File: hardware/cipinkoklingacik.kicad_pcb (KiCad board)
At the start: 2 copper layers, 100 x 85 mm, 96 parts, among them J1 GLITCH/GND, J2 TARGET/GND, J3 RESET/GND, J4 TRIGGER/GND, J5 UART, Q1 AO3400A, Q2 Si2377EDS, Q3 Si2377EDS, Q4 2N7002, Q5 2N7002, Q6 2N7002, U1 Raspberry Pi Pico 2, U2 UCC27517DBVR, U3 NX3L1T3157GMZ, U4 AP2112K-3.3, U5 AP2112K-1.8, U6 TLV70436DBVR, U7 SN74LVC1G17, U8 SN74AXC4T774PWR

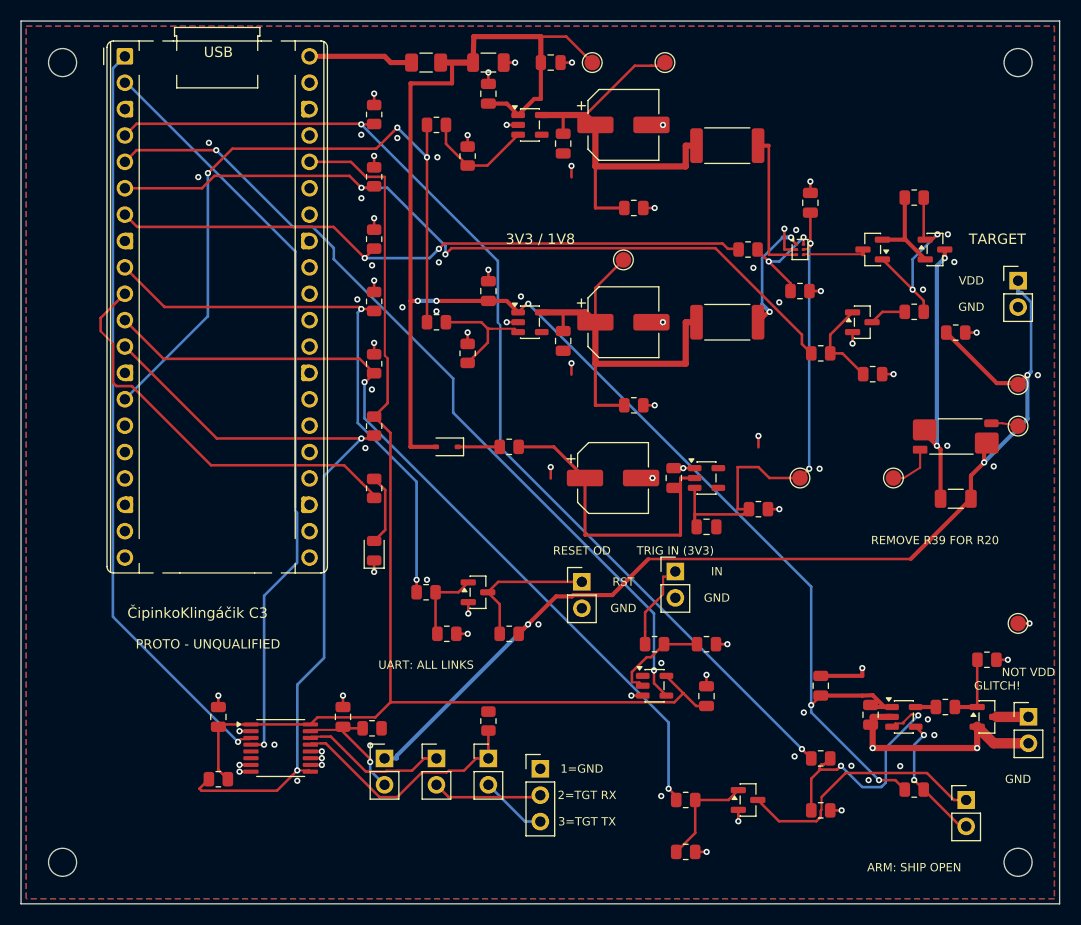
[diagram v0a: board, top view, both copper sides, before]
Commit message: Prepare C4 alpha.2 with stocked sourcing and DFM audit fixes
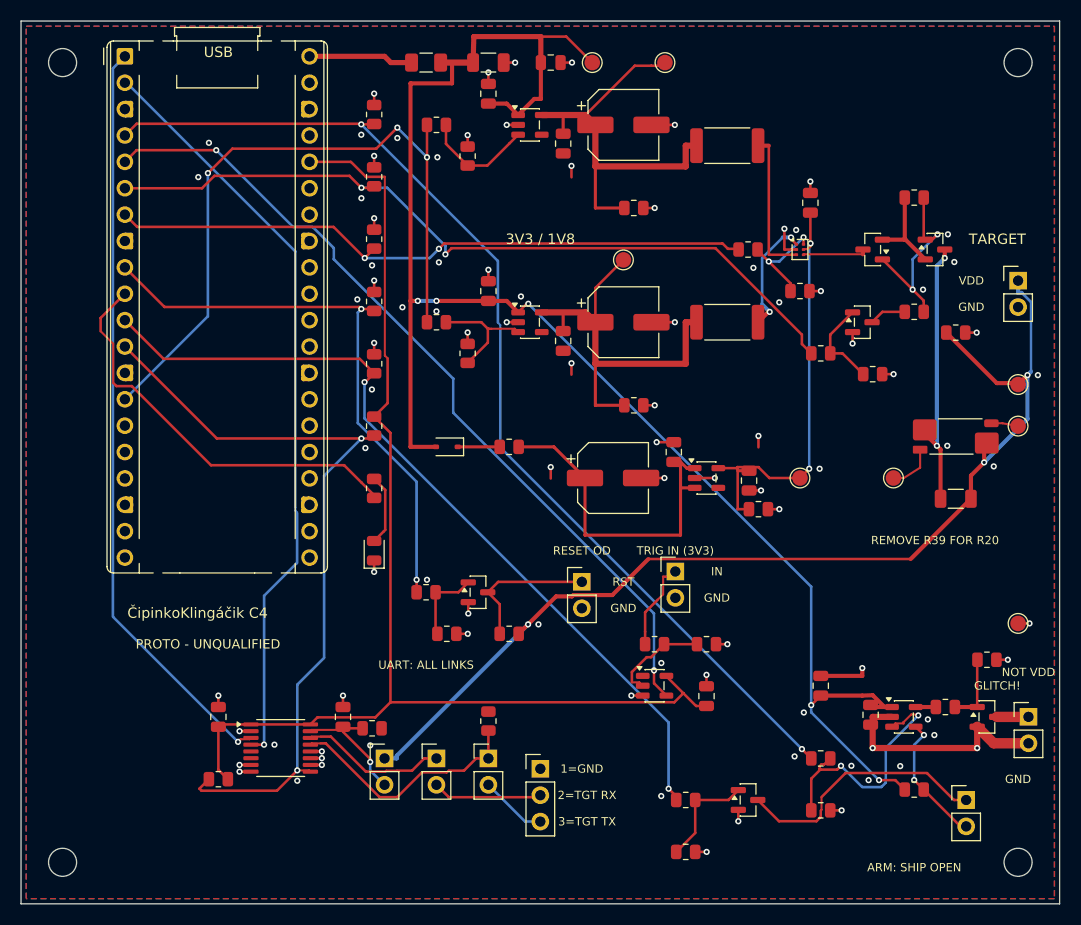
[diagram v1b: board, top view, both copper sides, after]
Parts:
- R15, R16: value 15 1% >=1W -> 15 1% 2W
- U6: value TLV70436DBVR -> TPS7A2036PDBVR
- moved C11 6.05 mm to (70.1, 44.2), turned to -90 degrees
- moved C10 2.50 mm to (62.9, 41.5)
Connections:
- U6 pad 1: /GND -> /HOLD
- U6 pad 2: /HOLD -> /GND
- U6 pad 3: /MVCC -> /HOLD
- U6 pad 5: unconnected-(U6-NC-Pad5) -> /MVCC
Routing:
- net /GND: track 83.3 -> 90.4 mm, vias 90 -> 92
- net /MVCC: track 47.9 -> 41.6 mm
- net /HOLD: track 29.8 -> 33.0 mm
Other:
- board text added: "ČipinkoKlingáčik C4"
- board text removed: "ČipinkoKlingáčik C3"
